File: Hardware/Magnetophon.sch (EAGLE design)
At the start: 22 parts, among them U2 TL072_

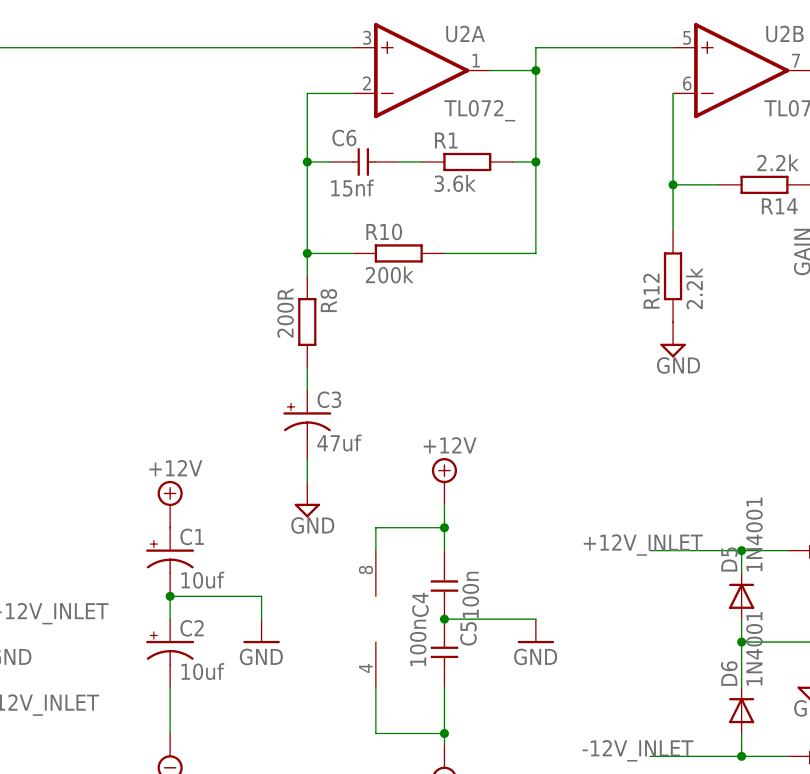
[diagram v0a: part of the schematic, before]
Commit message: add 10n cap and reroute
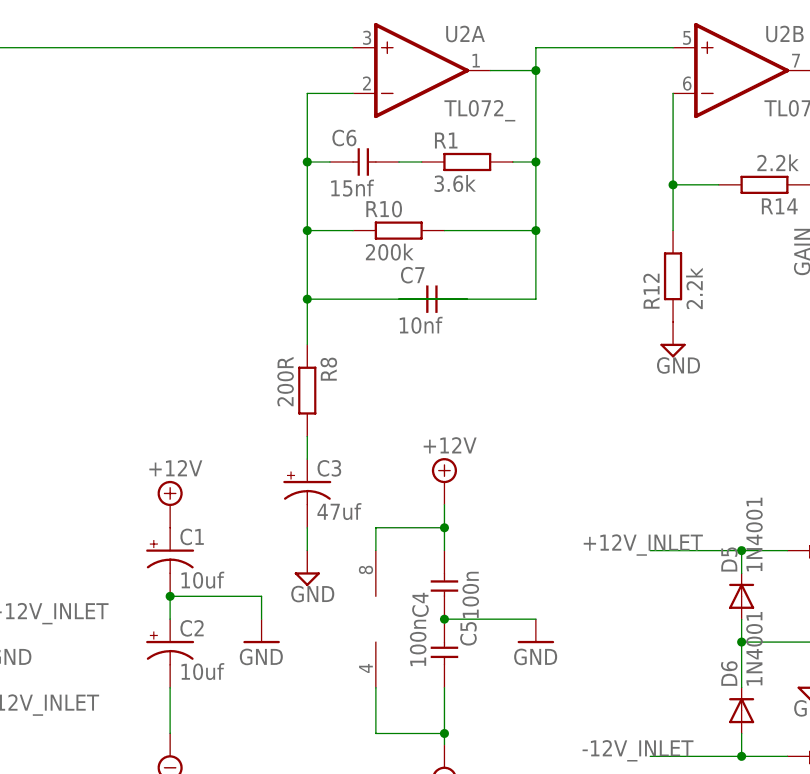
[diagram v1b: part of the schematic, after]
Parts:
- added C7: 10nf, TomW:C-EU050-024X044
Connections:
- net N$3: now also C7.1
- net N$4: now also C7.2
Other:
- moved on the sheet: C3, R10, R8
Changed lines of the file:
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@@
 <part name="U2" library="MusicThingModular" deviceset="TL072" device="_"/>
 <part name="U$2" library="MusicThingModular" deviceset="EURO_POWER_LOCK" device=""/>
+<part name="C7" library="TomW" deviceset="C-EU" device="050-024X044" value="10nf"/>
 </parts>
 <sheets>
@@
 <instance part="R16" gate="G$1" x="190.5" y="127" rot="R180"/>
 <instance part="SUPPLY7" gate="GND" x="200.66" y="116.84"/>
-<instance part="R8" gate="G$1" x="116.84" y="99.06" rot="R270"/>
-<instance part="R10" gate="G$1" x="127" y="106.68"/>
-<instance part="SUPPLY9" gate="GND" x="116.84" y="78.74"/>
+<instance part="R8" gate="G$1" x="116.84" y="91.44" rot="R270"/>
+<instance part="R10" gate="G$1" x="127" y="109.22"/>
+<instance part="SUPPLY9" gate="GND" x="116.84" y="71.12"/>
 <instance part="R12" gate="G$1" x="157.48" y="104.14" rot="R90"/>
 <instance part="SUPPLY5" gate="GND" x="157.48" y="96.52"/>
@@
 <instance part="U$1" gate="G$1" x="45.72" y="116.84"/>
 <instance part="SUPPLY1" gate="GND" x="55.88" y="109.22"/>
-<instance part="C3" gate="G$1" x="116.84" y="88.9"/>
+<instance part="C3" gate="G$1" x="116.84" y="81.28"/>
 <instance part="C6" gate="G$1" x="124.46" y="116.84" rot="R270"/>
 <instance part="R1" gate="G$1" x="134.62" y="116.84"/>
@@
 <instance part="U2" gate="P" x="124.46" y="66.04"/>
 <instance part="U$2" gate="G$1" x="73.66" y="60.96"/>
+<instance part="C7" gate="G$1" x="132.08" y="101.6" rot="R270"/>
 </instances>
 <busses>
@@
 <pinref part="C3" gate="G$1" pin="-"/>
 <pinref part="SUPPLY9" gate="GND" pin="GND"/>
-<wire x1="116.84" y1="83.82" x2="116.84" y2="81.28" width="0.1524" layer="91"/>
+<wire x1="116.84" y1="76.2" x2="116.84" y2="73.66" width="0.1524" layer="91"/>
 </segment>
 </net>
@@
 <junction x="142.24" y="127"/>
 <pinref part="R10" gate="G$1" pin="2"/>
-<wire x1="142.24" y1="116.84" x2="142.24" y2="106.68" width="0.1524" layer="91"/>
-<wire x1="132.08" y1="106.68" x2="142.24" y2="106.68" width="0.1524" layer="91"/>
+<wire x1="142.24" y1="116.84" x2="142.24" y2="109.22" width="0.1524" layer="91"/>
+<wire x1="132.08" y1="109.22" x2="142.24" y2="109.22" width="0.1524" layer="91"/>
 <wire x1="142.24" y1="127" x2="142.24" y2="129.54" width="0.1524" layer="91"/>
 <pinref part="U2" gate="B" pin="+IN"/>
@@
 <wire x1="139.7" y1="116.84" x2="142.24" y2="116.84" width="0.1524" layer="91"/>
 <junction x="142.24" y="116.84"/>
+<pinref part="C7" gate="G$1" pin="2"/>
+<wire x1="127" y1="101.6" x2="142.24" y2="101.6" width="0.1524" layer="91"/>
+<wire x1="142.24" y1="101.6" x2="142.24" y2="109.22" width="0.1524" layer="91"/>
+<junction x="142.24" y="109.22"/>
 </segment>
 </net>
@@
 <segment>
 <pinref part="U2" gate="A" pin="-IN"/>
-<wire x1="116.84" y1="106.68" x2="116.84" y2="116.84" width="0.1524" layer="91"/>
+<wire x1="116.84" y1="109.22" x2="116.84" y2="116.84" width="0.1524" layer="91"/>
 <wire x1="116.84" y1="116.84" x2="116.84" y2="124.46" width="0.1524" layer="91"/>
 <wire x1="116.84" y1="124.46" x2="121.92" y2="124.46" width="0.1524" layer="91"/>
 <pinref part="R10" gate="G$1" pin="1"/>
-<wire x1="121.92" y1="106.68" x2="116.84" y2="106.68" width="0.1524" layer="91"/>
+<wire x1="121.92" y1="109.22" x2="116.84" y2="109.22" width="0.1524" layer="91"/>
 <pinref part="R8" gate="G$1" pin="1"/>
-<wire x1="116.84" y1="104.14" x2="116.84" y2="106.68" width="0.1524" layer="91"/>
-<junction x="116.84" y="106.68"/>
+<wire x1="116.84" y1="96.52" x2="116.84" y2="101.6" width="0.1524" layer="91"/>
+<junction x="116.84" y="109.22"/>
 <pinref part="C6" gate="G$1" pin="2"/>
+<wire x1="116.84" y1="101.6" x2="116.84" y2="109.22" width="0.1524" layer="91"/>
 <wire x1="119.38" y1="116.84" x2="116.84" y2="116.84" width="0.1524" layer="91"/>
 <junction x="116.84" y="116.84"/>
+<pinref part="C7" gate="G$1" pin="1"/>
+<wire x1="134.62" y1="101.6" x2="116.84" y2="101.6" width="0.1524" layer="91"/>
+<junction x="116.84" y="101.6"/>
 </segment>
 </net>
@@
 <pinref part="C3" gate="G$1" pin="+"/>
 <pinref part="R8" gate="G$1" pin="2"/>
-<wire x1="116.84" y1="91.44" x2="116.84" y2="93.98" width="0.1524" layer="91"/>
-</segment>
-</net>
+<wire x1="116.84" y1="83.82" x2="116.84" y2="86.36" width="0.1524" layer="91"/>
+</segment>
+</net>

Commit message: improved layout and curves
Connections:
- net N$1 renamed FROMHEAD
- net N$2 renamed TOAMP
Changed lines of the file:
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@@
 <class number="0" name="default" width="0.3048" drill="0">
 </class>
-<class number="1" name="power" width="0.6096" drill="0">
+<class number="1" name="power" width="0.4064" drill="0">
 </class>
-<class number="2" name="ground" width="0.6096" drill="0">
+<class number="2" name="ground" width="0.4064" drill="0">
 </class>
 </classes>
@@
 </segment>
 </net>
-<net name="N$2" class="0">
+<net name="TOAMP" class="0">
 <segment>
 <wire x1="66.04" y1="121.92" x2="66.04" y2="129.54" width="0.1524" layer="91"/>
@@
 </segment>
 </net>
-<net name="N$1" class="0">
+<net name="FROMHEAD" class="0">
 <segment>
 <pinref part="U$1" gate="G$1" pin="P$1"/>

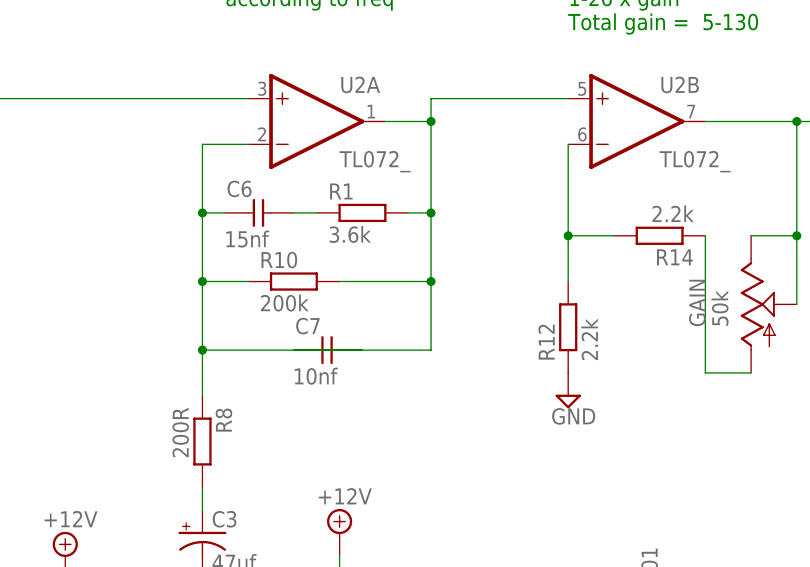
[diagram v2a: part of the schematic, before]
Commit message: Small board tweaks, fixes #1, fixes #2, fixes #3, fixes #4
#1 and #2 fixed by improved layout, #3 and #4 with tweaks here
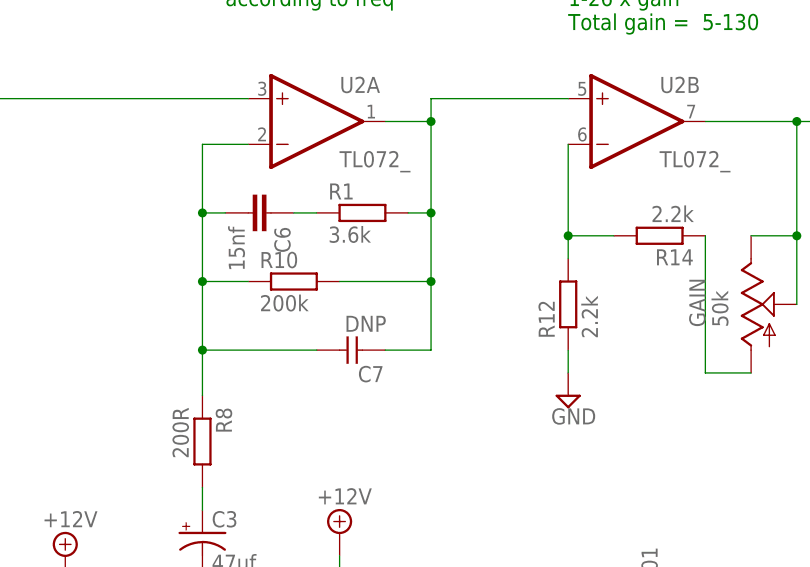
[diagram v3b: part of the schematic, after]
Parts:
- C6: device TomW:C-EU050-024X044 -> rcl:C-EU050-030X075
- C7: value 10nf -> DNP
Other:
- moved on the sheet: C7, R12
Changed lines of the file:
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@@
 <?xml version="1.0" encoding="utf-8"?>
 <!DOCTYPE eagle SYSTEM "eagle.dtd">
-<eagle version="7.4.0">
+<eagle version="7.2.0">
 <drawing>
 <settings>
@@
 <part name="SUPPLY1" library="supply2" deviceset="GND" device=""/>
 <part name="C3" library="SparkFun-Passives" deviceset="CAP_POL" device="PTH2" value="47uf"/>
-<part name="C6" library="TomW" deviceset="C-EU" device="050-024X044" value="15nf"/>
+<part name="C6" library="rcl" deviceset="C-EU" device="050-030X075" value="15nf"/>
 <part name="R1" library="MusicThingModular" deviceset="RESISTOR" device="7MM" value="3.6k"/>
 <part name="EXT" library="MusicThingModular" deviceset="THONKICONN" device="NEW"/>
@@
 <part name="U2" library="MusicThingModular" deviceset="TL072" device="_"/>
 <part name="U$2" library="MusicThingModular" deviceset="EURO_POWER_LOCK" device=""/>
-<part name="C7" library="TomW" deviceset="C-EU" device="050-024X044" value="10nf"/>
+<part name="C7" library="TomW" deviceset="C-EU" device="050-024X044" value="DNP"/>
 </parts>
 <sheets>
@@
 <instance part="R10" gate="G$1" x="127" y="109.22"/>
 <instance part="SUPPLY9" gate="GND" x="116.84" y="71.12"/>
-<instance part="R12" gate="G$1" x="157.48" y="104.14" rot="R90"/>
+<instance part="R12" gate="G$1" x="157.48" y="106.68" rot="R90"/>
 <instance part="SUPPLY5" gate="GND" x="157.48" y="96.52"/>
 <instance part="GND21" gate="1" x="111.76" y="63.5"/>
@@
 <instance part="U2" gate="P" x="124.46" y="66.04"/>
 <instance part="U$2" gate="G$1" x="73.66" y="60.96"/>
-<instance part="C7" gate="G$1" x="132.08" y="101.6" rot="R270"/>
+<instance part="C7" gate="G$1" x="132.08" y="101.6" rot="R90"/>
 </instances>
 <busses>
@@
 <pinref part="R12" gate="G$1" pin="1"/>
 <pinref part="SUPPLY5" gate="GND" pin="GND"/>
+<wire x1="157.48" y1="101.6" x2="157.48" y2="99.06" width="0.1524" layer="91"/>
 </segment>
 <segment>
@@
 <junction x="142.24" y="116.84"/>
 <pinref part="C7" gate="G$1" pin="2"/>
-<wire x1="127" y1="101.6" x2="142.24" y2="101.6" width="0.1524" layer="91"/>
+<wire x1="137.16" y1="101.6" x2="142.24" y2="101.6" width="0.1524" layer="91"/>
 <wire x1="142.24" y1="101.6" x2="142.24" y2="109.22" width="0.1524" layer="91"/>
 <junction x="142.24" y="109.22"/>
@@
 <junction x="116.84" y="116.84"/>
 <pinref part="C7" gate="G$1" pin="1"/>
-<wire x1="134.62" y1="101.6" x2="116.84" y2="101.6" width="0.1524" layer="91"/>
+<wire x1="129.54" y1="101.6" x2="116.84" y2="101.6" width="0.1524" layer="91"/>
 <junction x="116.84" y="101.6"/>
 </segment>
@@
 <pinref part="R12" gate="G$1" pin="2"/>
 <pinref part="R14" gate="G$1" pin="2"/>
-<wire x1="157.48" y1="114.3" x2="157.48" y2="109.22" width="0.1524" layer="91"/>
+<wire x1="157.48" y1="114.3" x2="157.48" y2="111.76" width="0.1524" layer="91"/>
 <wire x1="162.56" y1="114.3" x2="157.48" y2="114.3" width="0.1524" layer="91"/>
 <junction x="157.48" y="114.3"/>

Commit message: update R12 to improve gain
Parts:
- R12: value 2.2k -> 470R
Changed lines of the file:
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@@
 <?xml version="1.0" encoding="utf-8"?>
 <!DOCTYPE eagle SYSTEM "eagle.dtd">
-<eagle version="7.2.0">
+<eagle version="7.4.0">
 <drawing>
 <settings>
@@
 <part name="R10" library="MusicThingModular" deviceset="RESISTOR" device="7MM" value="200k"/>
 <part name="SUPPLY9" library="supply2" deviceset="GND" device=""/>
-<part name="R12" library="MusicThingModular" deviceset="RESISTOR" device="7MM" value="2.2k"/>
+<part name="R12" library="MusicThingModular" deviceset="RESISTOR" device="7MM" value="470R"/>
 <part name="SUPPLY5" library="supply2" deviceset="GND" device=""/>
 <part name="GND21" library="supply1" deviceset="GND" device=""/>

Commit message: Schematic image
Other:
- note added: "Install 10nf capacitor in C7 if circuit doesn't work (Caused by inaudible high frequency oscillation)"
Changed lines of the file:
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@@
 fuses with jumper wire.
 Don't get it the wrong way around! </text>
+<text x="127" y="91.44" size="1.016" layer="91">Install 10nf capacitor in C7
+if circuit doesn't work
+(Caused by inaudible high
+frequency oscillation)</text>
 </plain>
 <instances>
